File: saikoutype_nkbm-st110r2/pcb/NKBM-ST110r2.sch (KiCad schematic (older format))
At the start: 25 parts

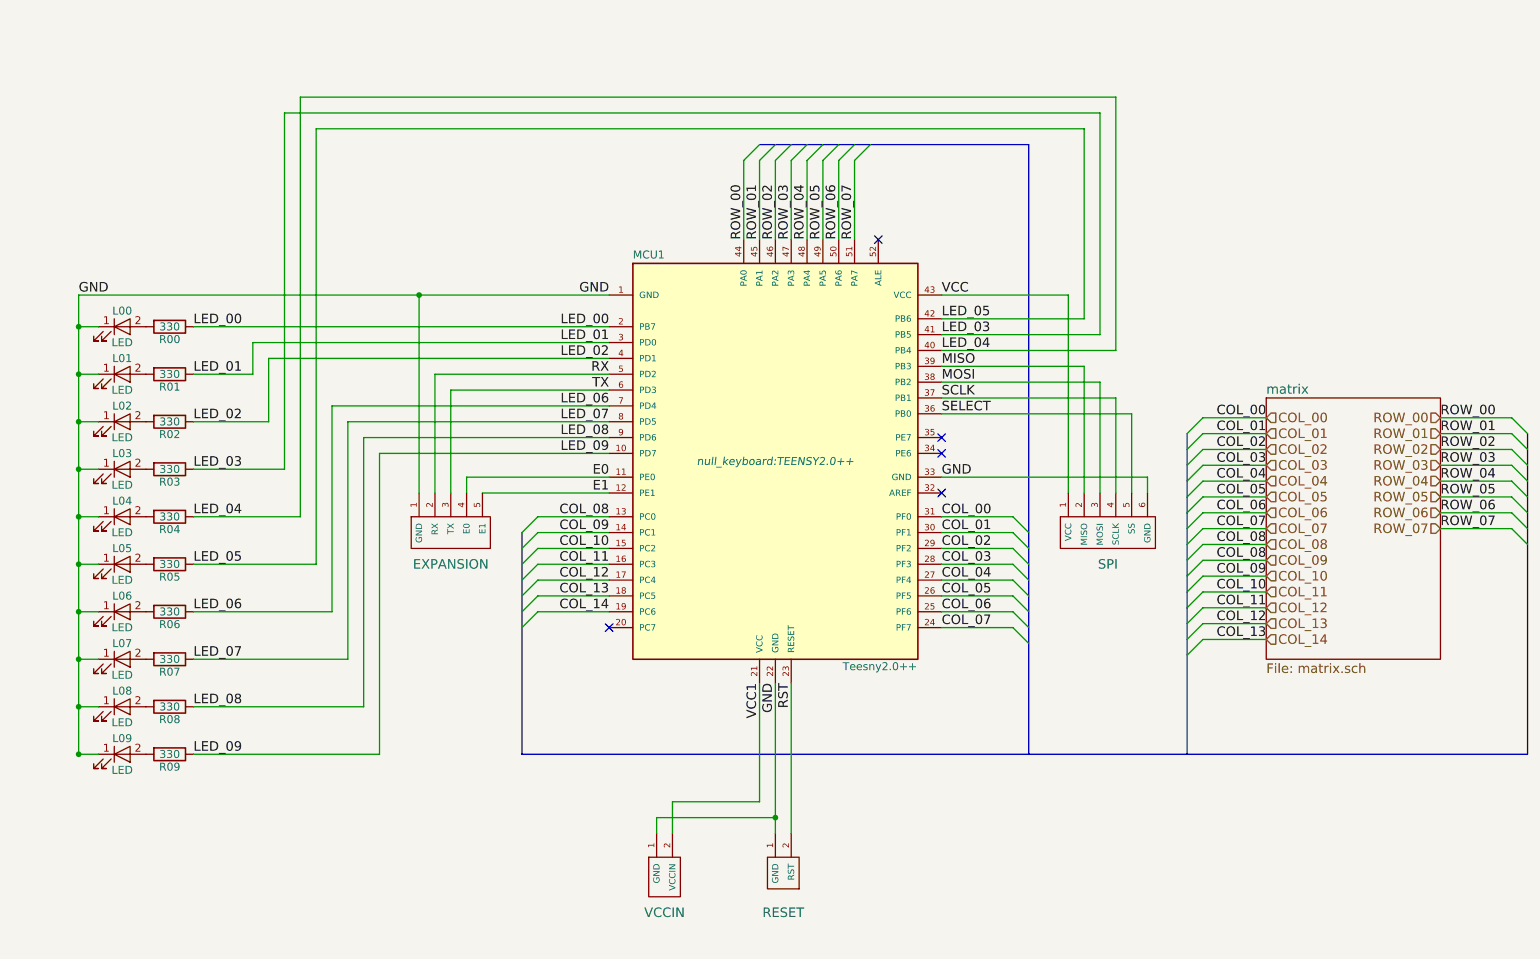
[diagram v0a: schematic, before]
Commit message: Fixed typo + updated schematic with graphics.
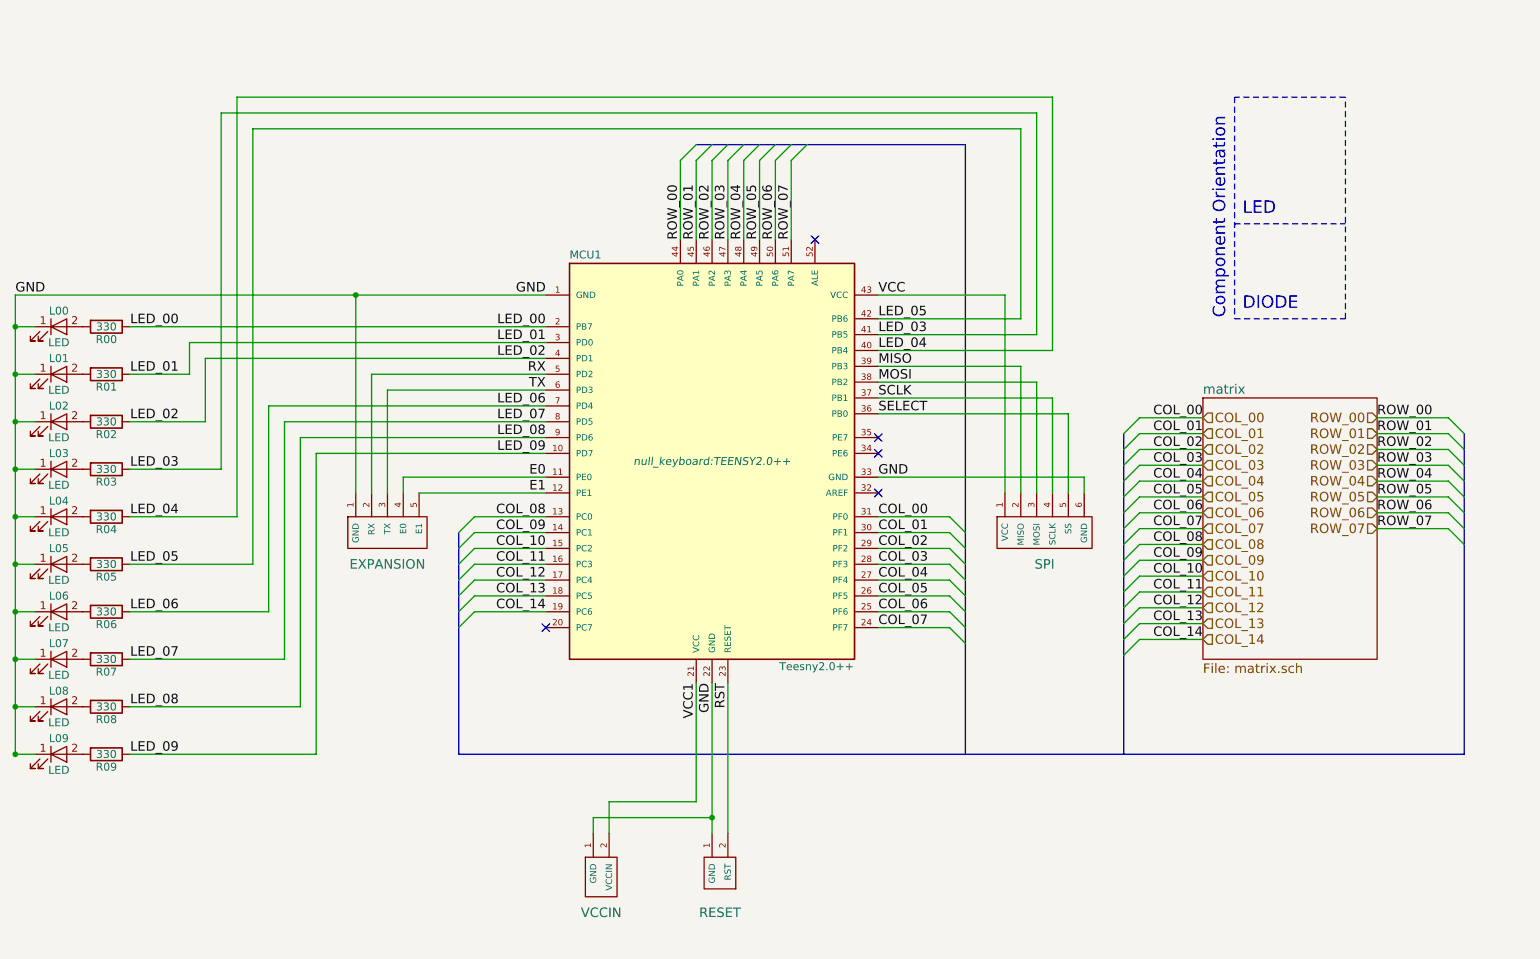
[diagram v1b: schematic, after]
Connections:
- net COL_08: no longer MCU1.14 (PC1), MCU1.15 (PC2), MCU1.16 (PC3), MCU1.17 (PC4), MCU1.18 (PC5), MCU1.19 (PC6)
- new net COL_09: MCU1.14 (PC1)
- new net COL_10: MCU1.15 (PC2)
- new net COL_11: MCU1.16 (PC3)
- new net COL_12: MCU1.17 (PC4)
- new net COL_13: MCU1.18 (PC5)
- new net COL_14: MCU1.19 (PC6)
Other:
- note added: "Component Orientation"
- note added: "DIODE"
- note added: "LED"
- moved on the sheet: L00, L01, L02, L03, L04, L05, L06, L07, L08, L09, MCU1, R00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

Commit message: Release NKBM-ST110 r2.1 2018.05.08
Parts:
- added H?: USB_BREAKOUT, symbol USB_BREAKOUT
- added P?: USB_MINI_B, symbol USB_OTG
- added USB_POWER: SOLDER_JUMPER, SOLDER_BRIDGE, symbol GS2
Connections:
- net GND: now also H?.4 (GND), P?.5 (GND), P?.6 (shield)
- net VCC1: now also USB_POWER.1 (G1)
- new net: H?.1 (VCC), P?.1 (VBUS), USB_POWER.2 (G2)
- new net: H?.2 (D-), P?.2 (D-)
- new net: H?.3 (D+), P?.3 (D+)
- no-connect marks 5 -> 6
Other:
- moved on the sheet: L00, L01, L02, L03, L04, L05, L06, L07, L08, L09, MCU1, R00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
